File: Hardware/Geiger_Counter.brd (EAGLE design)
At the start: 108 x 45.7 mm, 55 parts, among them Q1 MPSA42, Q2 MPSA18, Q3 MMBT4403, Q4 MPSA18, U10 FT232RL-BASICSSOP, U17 AVR_SPI_PRG_6PTH, U7 TRANSFORMERAUDIO, X1 USBSMD

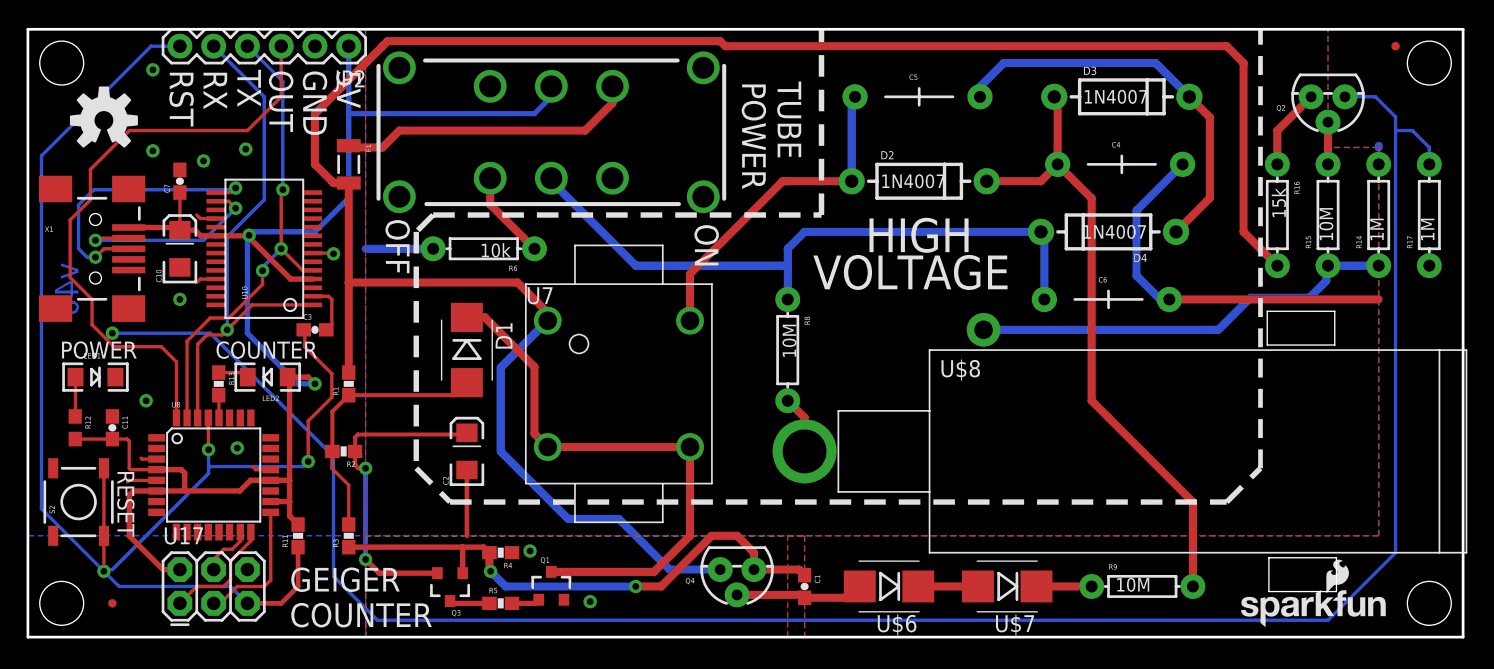
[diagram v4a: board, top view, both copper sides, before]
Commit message: added zip tie holes
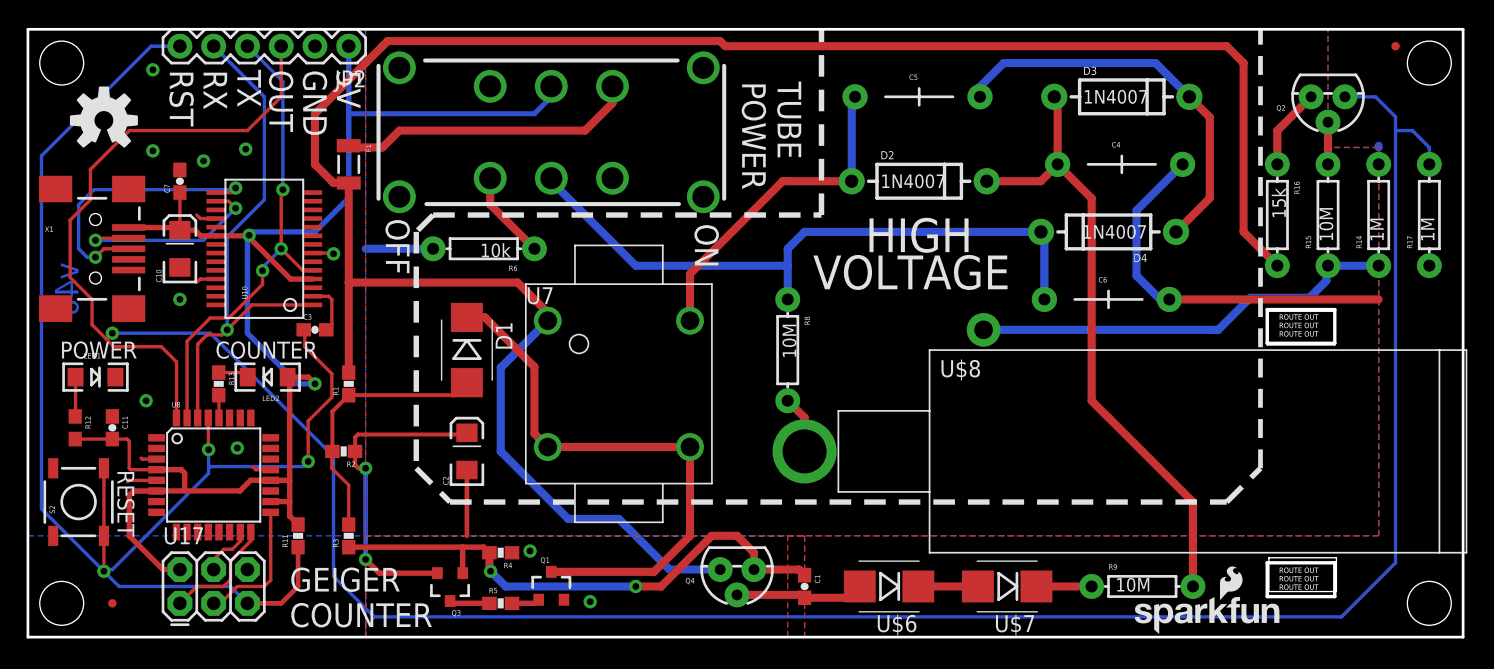
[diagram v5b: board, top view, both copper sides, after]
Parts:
- moved FRAME2 112.1 mm to (21.8, -19.1)
- moved LOGO2 8.02 mm to (82.8, 0.13)
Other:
- outline, holes or cut-outs redrawn
- board text added: "ROUTE OUT"
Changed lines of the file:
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@@
 <text x="52.07" y="-19.05" size="2.032" layer="51" font="vector" ratio="10">Aaron Weiss</text>
 <text x="33.2994" y="-21.7678" size="2.032" layer="51" font="vector" ratio="10">Revised by: Patrick Alberts</text>
+<wire x1="93.218" y1="24.638" x2="98.298" y2="24.638" width="0.254" layer="20"/>
+<wire x1="98.298" y1="24.638" x2="98.298" y2="22.098" width="0.254" layer="20"/>
+<wire x1="98.298" y1="22.098" x2="93.218" y2="22.098" width="0.254" layer="20"/>
+<wire x1="93.218" y1="22.098" x2="93.218" y2="24.638" width="0.254" layer="20"/>
+<wire x1="93.218" y1="5.588" x2="98.298" y2="5.588" width="0.254" layer="20"/>
+<wire x1="98.298" y1="5.588" x2="98.298" y2="3.048" width="0.254" layer="20"/>
+<wire x1="98.298" y1="3.048" x2="93.218" y2="3.048" width="0.254" layer="20"/>
+<wire x1="93.218" y1="3.048" x2="93.218" y2="5.588" width="0.254" layer="20"/>
+<text x="94.107" y="23.876" size="0.4064" layer="20" font="vector" ratio="15">ROUTE OUT</text>
+<text x="94.107" y="23.241" size="0.4064" layer="20" font="vector" ratio="15">ROUTE OUT</text>
+<text x="94.107" y="22.606" size="0.4064" layer="20" font="vector" ratio="15">ROUTE OUT</text>
+<text x="94.107" y="4.826" size="0.4064" layer="20" font="vector" ratio="15">ROUTE OUT</text>
+<text x="94.107" y="4.191" size="0.4064" layer="20" font="vector" ratio="15">ROUTE OUT</text>
+<text x="94.107" y="3.556" size="0.4064" layer="20" font="vector" ratio="15">ROUTE OUT</text>
 </plain>
 <attributes>
@@
 <element name="JP3" library="SparkFun" package="MICRO-FIDUCIAL" value="FIDUCIALUFIDUCIAL" x="102.87" y="44.45"/>
 <element name="LOGO1" library="SparkFun-Aesthetics" package="OSHW-LOGO-M" value="OSHW-LOGOM" x="5.715" y="38.862"/>
-<element name="LOGO2" library="SparkFun-Aesthetics" package="SFE_LOGO_NAME_FLAME_.1" value="SFE_LOGO_NAME_FLAME.1_INCH" x="90.805" y="0.635"/>
-<element name="FRAME2" library="SparkFun-Aesthetics" package="CREATIVE_COMMONS" value="FRAME-LEDGER" x="-88.70105625" y="0"/>
+<element name="LOGO2" library="SparkFun-Aesthetics" package="SFE_LOGO_NAME_FLAME_.1" value="SFE_LOGO_NAME_FLAME.1_INCH" x="82.804" y="0.127"/>
+<element name="FRAME2" library="SparkFun-Aesthetics" package="CREATIVE_COMMONS" value="FRAME-LEDGER" x="21.78894375" y="-19.05"/>
 </elements>
 <signals>
@@
 <wire x1="3.175" y1="27.051" x2="3.175" y2="31.369" width="0.254" layer="1"/>
 <wire x1="16.51" y1="38.1" x2="19.05" y2="40.64" width="0.254" layer="1"/>
-<wire x1="102.87" y1="6.35" x2="102.87" y2="38.1" width="0.254" layer="16"/>
+<wire x1="102.87" y1="5.588" x2="102.87" y2="38.1" width="0.254" layer="16"/>
 <wire x1="102.87" y1="38.1" x2="102.87" y2="39.13" width="0.254" layer="16"/>
 <wire x1="6.35" y1="22.86" x2="13.716" y2="22.86" width="0.254" layer="16"/>
 <wire x1="13.716" y1="22.86" x2="22.987" y2="13.589" width="0.254" layer="16"/>
 <wire x1="22.987" y1="13.589" x2="22.987" y2="4.572" width="0.254" layer="16"/>
-<wire x1="22.987" y1="4.572" x2="26.289" y2="1.27" width="0.254" layer="16"/>
 <contactref element="Q2" pad="1"/>
 <contactref element="R17" pad="P$2"/>
@@
 <wire x1="105.41" y1="36.83" x2="104.14" y2="38.1" width="0.254" layer="16"/>
 <wire x1="104.14" y1="38.1" x2="102.87" y2="38.1" width="0.254" layer="16"/>
-<wire x1="102.87" y1="6.35" x2="97.79" y2="1.27" width="0.254" layer="16"/>
-<wire x1="97.79" y1="1.27" x2="26.289" y2="1.27" width="0.254" layer="16"/>
+<wire x1="102.87" y1="5.588" x2="98.806" y2="1.524" width="0.254" layer="16"/>
+<wire x1="98.806" y1="1.524" x2="26.035" y2="1.524" width="0.254" layer="16"/>
+<wire x1="26.035" y1="1.524" x2="22.987" y2="4.572" width="0.254" layer="16"/>
 </signal>
 <signal name="MISO">

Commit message: added regular fiducial
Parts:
- removed JP1, JP3: FIDUCIALUFIDUCIAL, SparkFun:MICRO-FIDUCIAL
- added FID1, FID2: FIDUCIAL1X2, SparkFun-Aesthetics:FIDUCIAL-1X2
